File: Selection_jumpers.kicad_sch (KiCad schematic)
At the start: 7 parts, among them J10 U2RS485_TX, J17 U2RS485_DE_~{RE}, J17 U2RS485_RX, J6 R4_TX, J7 R4_RX

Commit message: Merge changes upstream
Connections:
- net U2U_RX: no longer J17.2 (Pin_2)
- net U2U_TX: no longer J10.2 (Pin_2)
- new net U2U_CH340_RX: J17.2 (Pin_2)
- new net U2U_CH340_TX: J10.2 (Pin_2)
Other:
- note added: "JUMPER FOR USING RS-485"
- note removed: "JUMPER FOR USING RS-485 with MCU pins"
- note removed: "JUMPER FOR USING USB to UART Using CH340"
- moved on the sheet: J6, J7

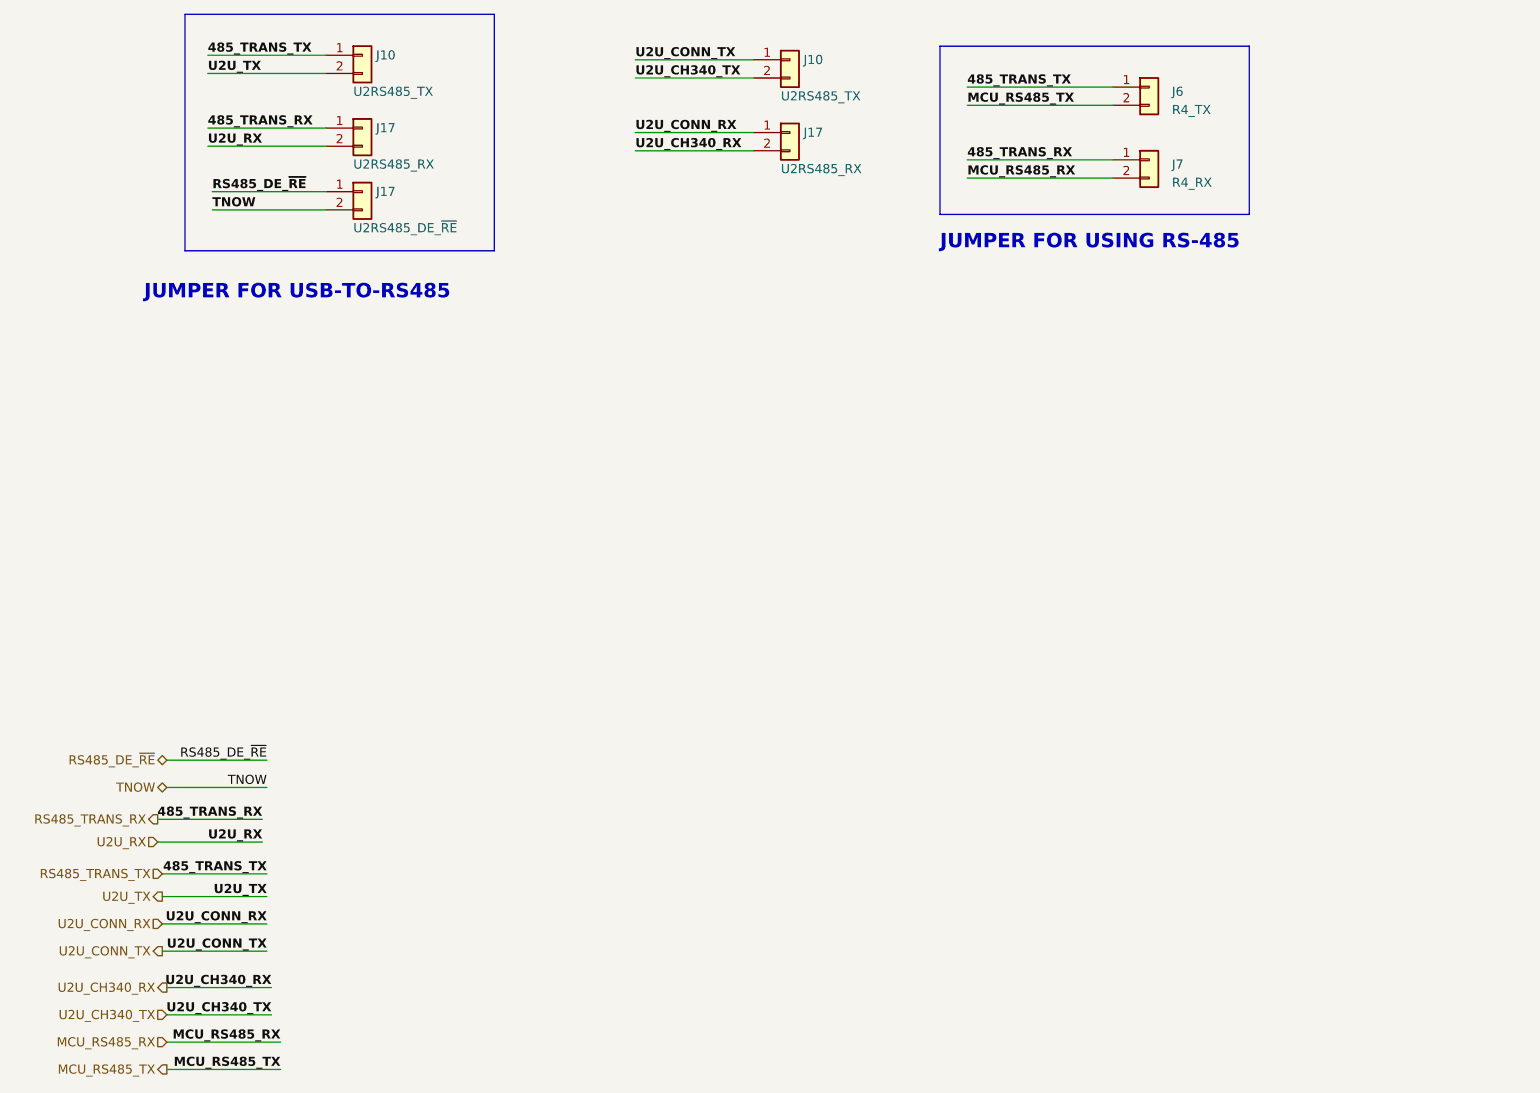
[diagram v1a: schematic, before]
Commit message: Completed routing for all GPIO pins
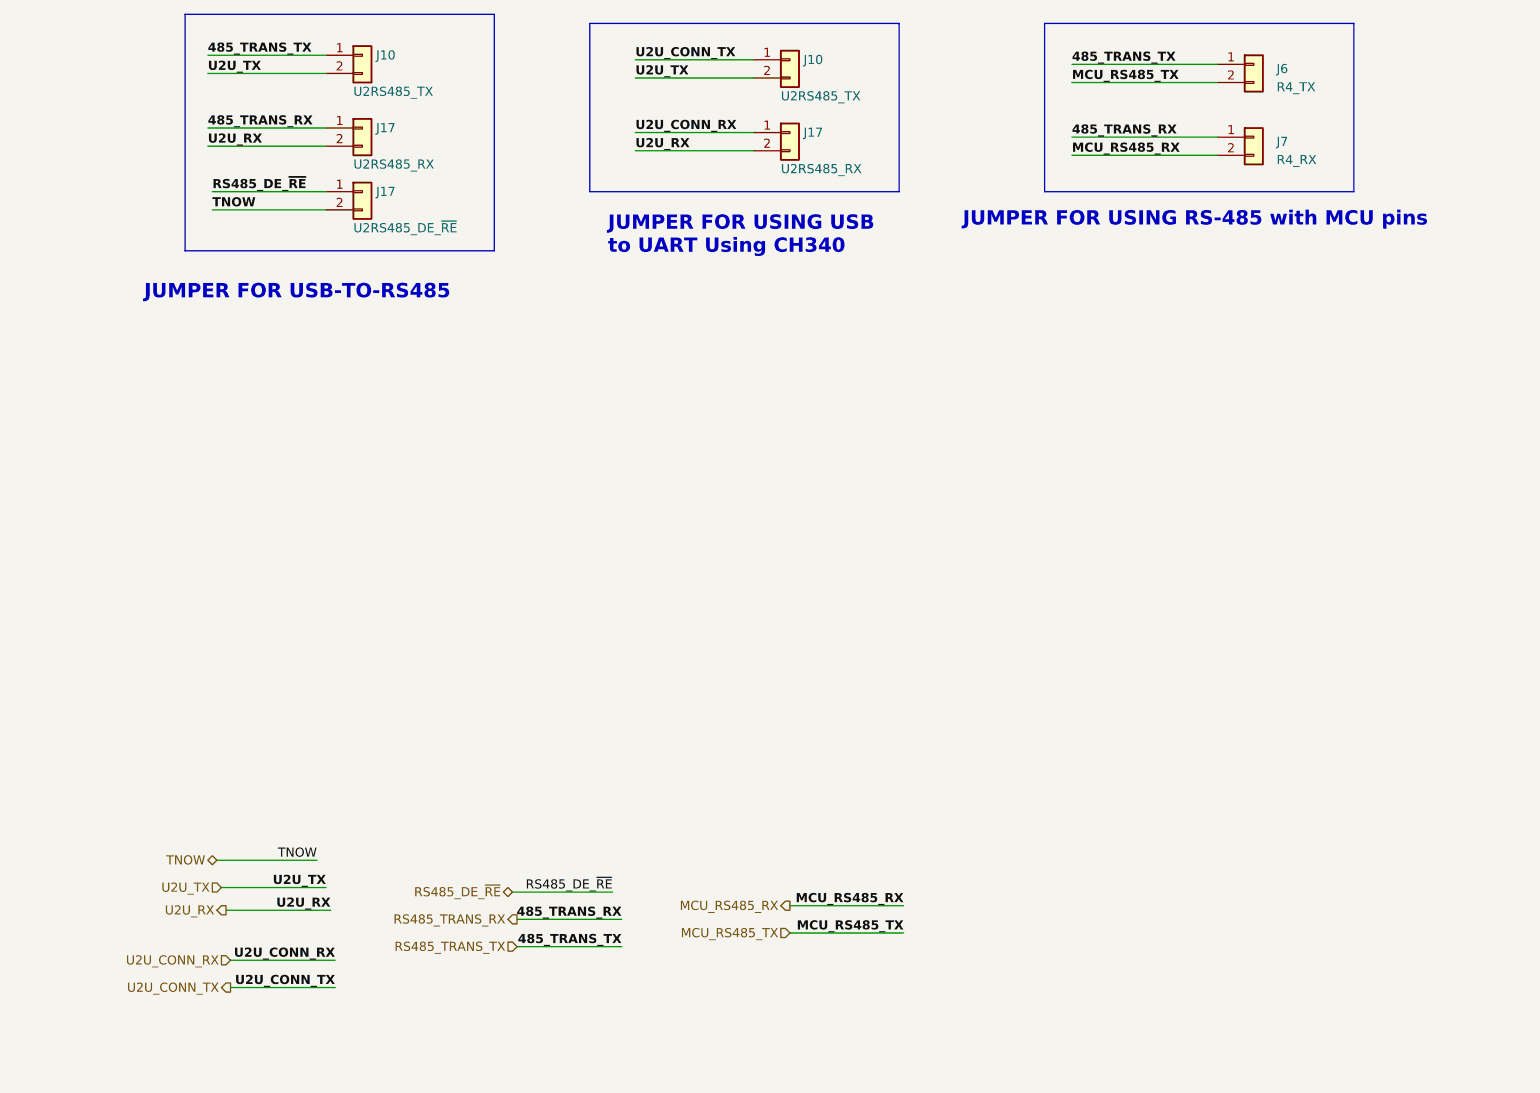
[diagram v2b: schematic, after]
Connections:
- net U2U_CH340_RX is gone; now on net U2U_RX: J17.2 (Pin_2)
- net U2U_CH340_TX is gone; now on net U2U_TX: J10.2 (Pin_2)
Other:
- note added: "JUMPER FOR USING RS-485 with MCU pins"
- note added: "JUMPER FOR USING USB to UART Using CH340"
- note removed: "JUMPER FOR USING RS-485"
- moved on the sheet: J6, J7
